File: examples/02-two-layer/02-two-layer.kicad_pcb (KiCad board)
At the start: 2 copper layers, 52.1 x 46.4 mm, 15 parts, among them P1 IN, P2 OUT, P3 POWER, P4 CONN_2, P5 MOUNTING_HOLE, P6 MOUNTING_HOLE, P7 MOUNTING_HOLE, P8 MOUNTING_HOLE, U1 ECC83

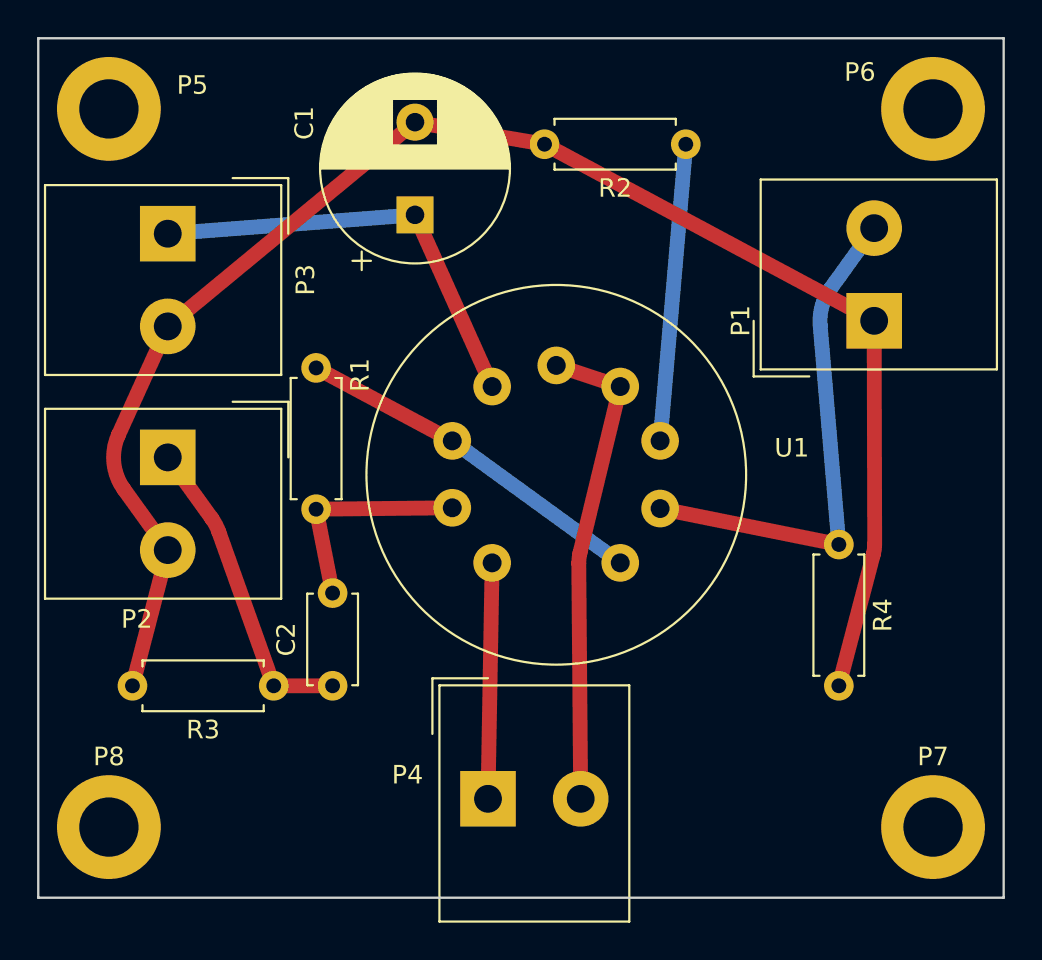
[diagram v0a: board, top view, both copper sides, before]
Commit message: feat(obstacles): convex shapes instead of enclosing circles
An obstacle is now a convex polygon inflated by the clearance radius --
the Minkowski sum of the polygon with a disc. Its boundary is the
polygon's edges pushed outward, joined by arcs on circles centred at its
*vertices*, so the taut path is still lines and arcs. One representation
covers the board: 1 vertex is a disc (round pad, via), 2 a capsule
(track segment, oval pad), 4 a rounded rectangle (rect pad).

The enclosing circle over-covered a long pad by up to sqrt(2) in every
direction -- room the router could not use and connections it refused
that would have fitted. A finished track also cost ~44 chained discs
where it now costs one capsule.

Two real bugs surfaced while testing this on a denser board.

**Pad orientation was 90 degrees out.** The angle in a pad's
(at x y angle) is the pad's *absolute* orientation, not an offset to add
to its footprint's. Adding them is wrong by exactly the footprint angle,
which turns a tall pad into a wide one. Pinned empirically by a property
the boards guarantee -- KiCad reports no overlapping pads on these
demos, so a correct model cannot invent any. Adding the angles invents
26 pad-pad overlaps on sonde xilinx; the pad's own angle invents none.
This one bug accounted for 20 of 23 DRC errors, and it also cost an
hour chasing a solder-mask theory that turned out to be a symptom.

**Copper graphics were not obstacles at all.** Boards carry text drawn
directly on copper layers; it belongs to no net, so copper must clear
it. Missing them was worth a clearance violation apiece.

Also: arcs flatter than 5 um of sagitta are now emitted as their chord.
KiCad rebuilds an arc from three points, and when those are nearly
collinear the reconstruction is ill-conditioned enough that a nanometre
of rounding can flip the sweep -- turning a 12 um sliver into copper
that loops most of the way round a circle.

Results, all judged by kicad-cli:

  ecc83-pp   F.Cu         17/20 -> 19/2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
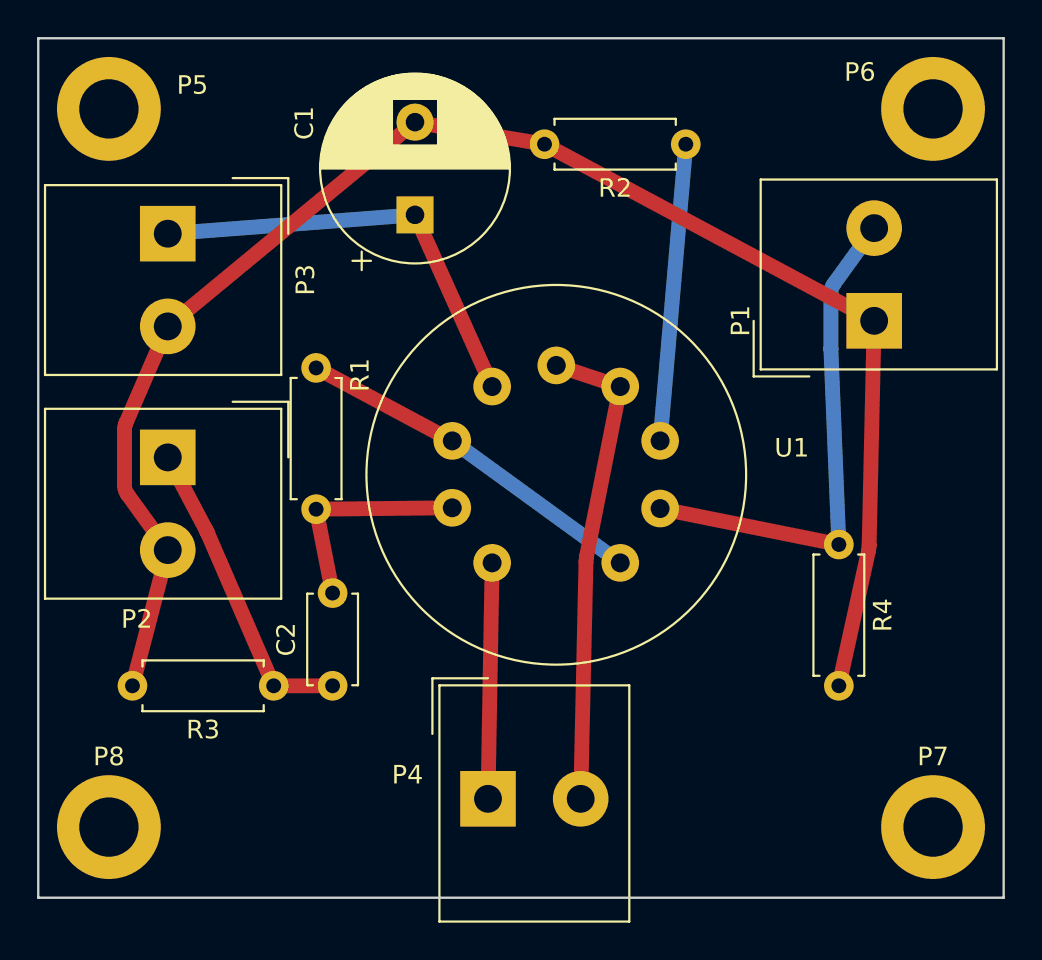
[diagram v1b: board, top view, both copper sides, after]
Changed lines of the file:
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@@
 	(segment
 		(start 150.542 131.191)
-		(end 150.437649 118.483372)
+		(end 150.826459 118.423814)
 		(width 0.8)
 		(layer "F.Cu")
@@
 	)
 	(arc
-		(start 150.437649 118.483372)
-		(mid 150.45226 118.209056)
-		(end 150.500378 117.938598)
+		(start 150.826459 118.423814)
+		(mid 150.836968 118.263904)
+		(end 150.861284 118.105505)
 		(width 0.8)
 		(layer "F.Cu")
@@
 	)
 	(segment
-		(start 150.500378 117.938598)
+		(start 150.861284 118.105505)
 		(end 152.675 108.955)
 		(width 0.8)
@@
 	(segment
 		(start 166.37 105.41)
-		(end 166.398366 117.470453)
+		(end 166.098589 117.511637)
 		(width 0.8)
 		(layer "F.Cu")
@@
 	)
 	(arc
-		(start 166.398366 117.470453)
-		(mid 166.382779 117.720047)
-		(end 166.335105 117.965541)
+		(start 166.098589 117.511637)
+		(mid 166.087392 117.669424)
+		(end 166.06099 117.825388)
 		(width 0.8)
 		(layer "F.Cu")
@@
 	)
 	(segment
-		(start 166.335105 117.965541)
+		(start 166.06099 117.825388)
 		(end 164.465 125.095)
 		(width 0.8)
@@
 	(segment
 		(start 164.465 117.475)
-		(end 163.457253 105.658406)
+		(end 164.036689 106.943892)
+		(width 0.8)
+		(layer "B.Cu")
+		(net 5)
+	)
+	(segment
+		(start 164.036689 106.943892)
+		(end 164.036 106.91)
+		(width 0.8)
+		(layer "B.Cu")
+		(net 5)
+	)
+	(segment
+		(start 164.036 106.91)
+		(end 164.036 103.91)
 		(width 0.8)
 		(layer "B.Cu")
@@
 	)
 	(arc
-		(start 163.457253 105.658406)
-		(mid 163.552351 104.631119)
-		(end 163.998382 103.70084)
+		(start 164.036 103.91)
+		(mid 164.076482 103.653318)
+		(end 164.193999 103.421555)
 		(width 0.8)
 		(layer "B.Cu")
@@
 	)
 	(segment
-		(start 163.998382 103.70084)
+		(start 164.193999 103.421555)
 		(end 166.37 100.41)
 		(width 0.8)
@@
 	(segment
 		(start 133.985 125.095)
-		(end 131.023338 116.79369)
-		(width 0.8)
-		(layer "F.Cu")
-		(net 3)
-	)
-	(arc
-		(start 131.023338 116.79369)
-		(mid 130.858121 116.416798)
-		(end 130.641618 116.06684)
+		(end 130.411602 116.848046)
 		(width 0.8)
 		(layer "F.Cu")
@@
 	)
 	(segment
-		(start 130.641618 116.06684)
+		(start 130.411602 116.848046)
+		(end 130.334103 116.686489)
+		(width 0.8)
+		(layer "F.Cu")
+		(net 3)
+	)
+	(segment
+		(start 130.334103 116.686489)
 		(end 128.27 112.776)
 		(width 0.8)
@@
 	(segment
 		(start 128.27 105.711)
-		(end 125.60867 111.566403)
+		(end 126.004622 110.944711)
 		(width 0.8)
 		(layer "F.Cu")
@@
 	)
 	(arc
-		(start 125.60867 111.566403)
-		(mid 125.360975 113.064746)
-		(end 125.898382 114.48516)
+		(start 126.004622 110.944711)
+		(mid 125.953336 111.106839)
+		(end 125.936 111.276)
 		(width 0.8)
 		(layer "F.Cu")
@@
 	)
 	(segment
-		(start 125.898382 114.48516)
+		(start 125.936 111.276)
+		(end 125.936 114.276)
+		(width 0.8)
+		(layer "F.Cu")
+		(net 1)
+	)
+	(arc
+		(start 125.936 114.276)
+		(mid 125.976482 114.532682)
+		(end 126.093999 114.764445)
+		(width 0.8)
+		(layer "F.Cu")
+		(net 1)
+	)
+	(segment
+		(start 126.093999 114.764445)
 		(end 128.27 117.776)
 		(width 0.8)

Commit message: feat(bundle): route nets as a seated bundle rather than one after another
Sequential routing has a failure no ordering can fix. A gap wide enough
for two tracks: the first net through it is asked, alone, where a rubber
band would sit, and a rubber band sits in the middle. The second finds
the gap full. Re-routing the first puts it back exactly where it was --
the taut path is deterministic -- so ripping up and re-ordering only
swaps who is stranded.

Routing now happens in two stages. Every connection is first routed
against the static obstacles alone, which says which gap it *wants* --
including connections that a sequential pass would have blocked, so a
stranded net still gets a say. Gaps are then counted,
floor((D - c) / (w + c)) tracks each, contending nets are ordered across
each gap and given slots, and every connection is routed again against
obstacles inflated by its own slot's share. Nothing is pushed: each net
is simply handed a problem that already contains the others.

The slack in a gap has to be divided rather than handed to every net.
Giving each the full band let them all drift to the inside of it and end
up 1.5 apart where 2.0 was required; folding an equal share into the
stride fixes it, and any position in one band is then a full pitch from
any position in the next.

Slot assignment is a model, so the arrangement is verified afterwards on
real geometry and anything still too close is routed the old way. That
settling pass also reconsiders which layer a connection sits on --
choosing it before the contention is known left a two-layer board using
one layer and stranding a net on it.

Results are unchanged on all three boards, and that is the honest
finding rather than a disappointment to hide:

  ecc83-pp F.Cu        19/20 -> 19/20
  ecc83-pp F.Cu+B.Cu   20/20 -> 20/20
  sonde xilinx         63/66 -> 63/66, 0 DRC either way

The mechanism is proven on the case it exists for -- tests/test_bundle.py
shows the second net raising NoPathFound sequentiall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
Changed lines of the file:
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@@
 	(segment
 		(start 141.605 94.695)
+		(end 139.046033 96.591777)
+		(width 0.8)
+		(layer "F.Cu")
+		(net 1)
+	)
+	(segment
+		(start 139.046033 96.591777)
+		(end 138.913032 96.697209)
+		(width 0.8)
+		(layer "F.Cu")
+		(net 1)
+	)
+	(segment
+		(start 138.913032 96.697209)
 		(end 128.27 105.711)
 		(width 0.8)

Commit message: feat(relax): settle every band at once instead of counting gaps
Replaces the portal/capacity/slot machinery with the direct thing it was
approximating. A board's copper is one arrangement, not a sequence of
decisions, so every band is re-solved against the *previous* positions of
all the others and all of them move together. Two bands contending for
the same space now both give way, which no ordering or rip-up can
produce.

The portals were scaffolding built to fake simultaneity, and they only
ever covered contention inside a narrow gap between two static obstacles.
Measurement showed why that was not enough: contention costs 30.4% of
ideal length on ecc83-pp and the slot model recovered none of it, because
the bands that detour are detouring around other *bands*, in open copper,
where no such gap exists.

Which layer a band sits on is settled in the same loop. Fixing it
beforehand -- each connection taking whichever layer was shortest for it
alone -- puts every band on one face, which the relaxation is then good
enough to make work while being materially longer than spreading out.

An earlier version also annealed the band-to-band clearance from soft to
solid, arguing that the taut solver treats other copper as walls and
walls do not yield. The argument is sound and the effect is nil: the
finished route on ecc83-pp is identical at 0.30, 0.60 and 1.00 hardness.
Bands have room to go around each other far more often than they need to
pass through, so the softening is gone rather than kept on a plausible
story.

Sequential settling versus joint relaxation, same boards, same process:

  ecc83-pp F.Cu        19/20  305.3mm  ->  20/20  292.9mm
  ecc83-pp F.Cu+B.Cu   20/20  239.5mm  ->  20/20  239.5mm
  sonde xilinx         63/66  690.3mm  ->  64/66  678.4mm

Where there is headroom it wins on both counts -- more connections
finished and less copper -- which is the tell that it is doing the right
thing rather than merely doing something. Zero DRC errors throughout.

Relax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
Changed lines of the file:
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@@
 		(end 150.826459 118.423814)
 		(width 0.8)
-		(layer "F.Cu")
+		(layer "B.Cu")
 		(net 7)
 	)
@@
 		(end 150.861284 118.105505)
 		(width 0.8)
-		(layer "F.Cu")
+		(layer "B.Cu")
 		(net 7)
 	)
@@
 		(end 152.675 108.955)
 		(width 0.8)
-		(layer "F.Cu")
+		(layer "B.Cu")
 		(net 7)
 	)
@@
 		(end 166.37 105.41)
 		(width 0.8)
-		(layer "F.Cu")
+		(layer "B.Cu")
 		(net 1)
 	)
@@
 	(segment
 		(start 141.605 94.695)
-		(end 139.046033 96.591777)
-		(width 0.8)
-		(layer "F.Cu")
-		(net 1)
-	)
-	(segment
-		(start 139.046033 96.591777)
-		(end 138.913032 96.697209)
-		(width 0.8)
-		(layer "F.Cu")
-		(net 1)
-	)
-	(segment
-		(start 138.913032 96.697209)
 		(end 128.27 105.711)
 		(width 0.8)
-		(layer "F.Cu")
+		(layer "B.Cu")
 		(net 1)
 	)
@@
 		(end 164.036689 106.943892)
 		(width 0.8)
-		(layer "B.Cu")
+		(layer "F.Cu")
 		(net 5)
 	)
@@
 		(end 164.036 106.91)
 		(width 0.8)
-		(layer "B.Cu")
+		(layer "F.Cu")
 		(net 5)
 	)
@@
 		(end 164.036 103.91)
 		(width 0.8)
-		(layer "B.Cu")
+		(layer "F.Cu")
 		(net 5)
 	)
@@
 		(end 164.193999 103.421555)
 		(width 0.8)
-		(layer "B.Cu")
+		(layer "F.Cu")
 		(net 5)
 	)
@@
 		(end 166.37 100.41)
 		(width 0.8)
-		(layer "B.Cu")
+		(layer "F.Cu")
 		(net 5)
 	)
@@
 		(end 154.825 111.885)
 		(width 0.8)
-		(layer "B.Cu")
+		(layer "F.Cu")
 		(net 13)
 	)
@@
 		(end 130.411602 116.848046)
 		(width 0.8)
-		(layer "F.Cu")
+		(layer "B.Cu")
 		(net 3)
 	)
@@
 		(end 130.334103 116.686489)
 		(width 0.8)
-		(layer "F.Cu")
+		(layer "B.Cu")
 		(net 3)
 	)
@@
 		(end 128.27 112.776)
 		(width 0.8)
-		(layer "F.Cu")
+		(layer "B.Cu")
 		(net 3)
 	)
@@
 		(end 128.27 100.711)
 		(width 0.8)
-		(layer "B.Cu")
+		(layer "F.Cu")
 		(net 2)
 	)
@@
 		(end 152.675 118.465)
 		(width 0.8)
-		(layer "B.Cu")
+		(layer "F.Cu")
 		(net 12)
 	)
